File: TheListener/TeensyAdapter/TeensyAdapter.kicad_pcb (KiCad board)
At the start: 2 copper layers, 19 parts, among them J1 Conn_02x05_Odd_Even, J2 Conn_02x05_Odd_Even, U1 Teensy3.5

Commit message: updates
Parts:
- moved R16 6.00 mm to (159.0, 130.8), turned to 90 degrees
- moved R11 6.00 mm to (176.8, 140.2), turned to 270 degrees
- moved R4 6.00 mm to (153.9, 140.2), turned to 90 degrees
- moved R6 6.00 mm to (159.0, 140.2), turned to 90 degrees
- moved R8 6.00 mm to (164.1, 140.2), turned to 90 degrees
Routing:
- net R_8: track 0.00 -> 32.9 mm
- net T_6: track 22.0 -> 4.25 mm
- net R_4: track 10.0 -> 3.92 mm
- net T_7: track 14.2 -> 8.75 mm
- net T_3: track 11.1 -> 16.3 mm
- net T_1: track 5.73 -> 10.1 mm
- net R_7: track 10.2 -> 6.37 mm
- net R_1: track 0.00 -> 3.54 mm
- net R_2: track 17.9 -> 21.1 mm
- net T_4: track 12.9 -> 15.7 mm
- net R_6: track 32.4 -> 30.0 mm
- net Net-(R9-Pad1): track 2.34 -> 0.00 mm
- net Net-(R8-Pad1): track 2.34 -> 0.00 mm
- net Net-(R7-Pad1): track 2.34 -> 0.00 mm
- net Net-(R6-Pad1): track 2.34 -> 0.00 mm
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
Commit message: working
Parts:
- added J3: Conn_01x04_Male, Connector_PinHeader_2.54mm:PinHeader_1x04_P2.54mm_Vertical, F.Cu at (149.9, 139.7)
- added J4: Conn_01x04_Male, Connector_PinHeader_2.54mm:PinHeader_1x04_P2.54mm_Vertical, F.Cu at (175.3, 129.5)
- moved R16 7.09 mm to (157.5, 123.8), turned to 270 degrees
- moved R7 6.73 mm to (160.0, 139.7), turned to 90 degrees
- moved J1 6.13 mm to (154.9, 139.7)
- moved R11 5.27 mm to (175.3, 145.3), turned to 90 degrees
- moved R6 5.27 mm to (157.5, 145.3), turned to 270 degrees
- moved R4 5.27 mm to (152.4, 145.3), turned to 270 degrees
- moved R14 5.03 mm to (165.1, 129.5), turned to 270 degrees
- moved R5 1.83 mm to (154.9, 145.3)
- moved R1 1.82 mm to (144.8, 145.3)
- moved R2 1.82 mm to (147.3, 145.3)
- moved R9 1.82 mm to (165.1, 145.3)
- moved R10 1.82 mm to (170.2, 145.3)
- moved R3 1.82 mm to (149.9, 145.3)
- moved R13 1.81 mm to (167.6, 123.8)
- moved R15 1.81 mm to (154.9, 123.8)
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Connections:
- J1 pad 1: T_5 -> R_5
- J1 pad 2: R_5 -> T_6
- J1 pad 3: GND -> T_5
- J1 pad 4: T_6 -> R_6
- J1 pad 5: +5V -> (no net)
- J1 pad 6: R_6 -> (no net)
- J2 pad 1: T_1 -> R_1
- J2 pad 2: R_1 -> T_2
- J2 pad 3: GND -> T_1
- J2 pad 4: T_2 -> R_2
- J2 pad 5: +5V -> (no net)
- J2 pad 6: R_2 -> (no net)
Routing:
- net R_6: track 30.0 -> 1.82 mm
- net R_8: track 32.9 -> 17.4 mm
- net R_7: track 6.37 -> 17.4 mm
- net +5V: track 0.00 -> 9.72 mm
- net T_3: track 16.3 -> 6.99 mm
- net R_4: track 3.92 -> 10.3 mm
- net T_8: track 11.8 -> 6.07 mm
- net T_5: track 6.15 -> 10.5 mm
- net T_7: track 8.75 -> 12.8 mm
- net R_1: track 3.54 -> 6.86 mm
- net T_2: track 8.94 -> 6.28 mm
- net T_4: track 15.7 -> 13.1 mm
- net Net-(R3-Pad1): track 2.34 -> 0.00 mm
- net Net-(R2-Pad1): track 2.34 -> 0.00 mm
- net Net-(R14-Pad1): track 2.34 -> 0.00 mm
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
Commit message: working
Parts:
- moved R14 5.71 mm to (165.1, 123.8), turned to 90 degrees
- moved R7 5.59 mm to (160.0, 145.3), turned to 270 degrees
- moved R8 5.59 mm to (162.6, 145.3), turned to 270 degrees
- moved J2 5.08 mm to (165.1, 129.5)
- moved J3 5.08 mm to (144.8, 139.7)
- moved J1 5.08 mm to (149.9, 139.7)
- moved J4 5.08 mm to (170.2, 129.5)
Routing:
- net R_6: track 1.82 -> 16.9 mm
- net R_2: track 22.2 -> 10.2 mm
- net R_3: track 6.22 -> 18.1 mm
- net R_1: track 6.86 -> 18.3 mm
- net +5V: track 9.72 -> 0.00 mm
- net T_3: track 6.99 -> 16.1 mm
- net T_4: track 13.1 -> 6.07 mm
- net R_4: track 10.3 -> 17.2 mm
- net R_7: track 17.4 -> 10.5 mm
- net T_6: track 4.35 -> 9.68 mm
- net T_7: track 12.8 -> 8.00 mm
- net T_2: track 6.28 -> 10.4 mm
- net T_8: track 6.07 -> 9.97 mm
- net R_8: track 17.4 -> 15.2 mm
- net T_1: track 10.6 -> 8.83 mm
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
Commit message: updates
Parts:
- moved R3 6.86 mm to (149.9, 138.4), turned to 90 degrees
- moved R6 6.86 mm to (157.5, 138.4), turned to 90 degrees
- moved R7 6.86 mm to (160.0, 138.4), turned to 90 degrees
- moved R8 6.86 mm to (162.6, 138.4), turned to 90 degrees
- moved R16 4.45 mm to (157.5, 128.3), turned to 90 degrees
- moved J1 2.84 mm to (152.4, 138.4)
- moved J2 2.84 mm to (167.6, 128.3)
- moved J3 2.84 mm to (147.3, 138.4)
- moved J4 2.84 mm to (172.7, 128.3)
- moved R1 1.27 mm to (144.8, 144.0)
- moved R10 1.27 mm to (170.2, 144.0)
- moved R11 1.27 mm to (175.3, 144.0)
- moved R2 1.27 mm to (147.3, 144.0)
- moved R4 1.27 mm to (152.4, 144.0)
- moved R5 1.27 mm to (154.9, 144.0)
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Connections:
- U1 pad 1: (no net) -> GND
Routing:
- net GND: track 0.00 -> 11.4 mm
- net +5V: track 0.00 -> 10.4 mm
- net T_2: track 10.4 -> 1.56 mm
- net T_6: track 9.68 -> 1.92 mm
- net T_1: track 8.83 -> 2.58 mm
- net T_7: track 8.00 -> 2.17 mm
- net R_4: track 17.2 -> 11.6 mm
- net T_3: track 16.1 -> 10.5 mm
- net R_3: track 18.1 -> 13.2 mm
- net R_7: track 10.5 -> 15.1 mm
- net R_1: track 18.3 -> 22.4 mm
- net R_8: track 15.2 -> 11.1 mm
- net R_6: track 16.9 -> 13.9 mm
- net T_8: track 9.97 -> 7.66 mm
- net R_2: track 10.2 -> 12.2 mm
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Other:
- board outline added: 67.3 x 30 mm

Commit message: wip
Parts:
- removed J3, J4: Conn_01x04_Male, Connector_PinHeader_2.54mm:PinHeader_1x04_P2.54mm_Vertical
- moved R1 6.10 mm to (144.8, 137.9), turned to 90 degrees
- moved R3 0.51 mm to (149.9, 137.9)
- moved R6 0.51 mm to (157.5, 137.9)
- moved R7 0.51 mm to (160.0, 137.9)
- moved R8 0.51 mm to (162.6, 137.9)
- moved R16 0.51 mm to (157.5, 128.8)
- moved R12 0.13 mm to (172.7, 122.7)
- moved R13 0.13 mm to (167.6, 122.7)
- moved R14 0.13 mm to (165.1, 122.7)
- moved R15 0.13 mm to (154.9, 122.7)
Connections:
- J1 pad 5: (no net) -> +5V
- J1 pad 6: (no net) -> GND
- J2 pad 5: (no net) -> +5V
- J2 pad 6: (no net) -> GND
- R1 pad 2: R_8 -> R_4
- R10 pad 2: R_3 -> R_7
- R11 pad 1: R_4 -> R_8
- R12 pad 2: T_5 -> T_1
- R13 pad 2: R_5 -> R_1
- R14 pad 2: R_6 -> R_3
- R15 pad 1: T_8 -> T_4
- R16 pad 1: T_7 -> T_3
- R2 pad 2: R_7 -> R_5
- R3 pad 2: T_1 -> T_5
- R4 pad 2: R_1 -> R_2
- R5 pad 2: R_2 -> R_6
- R6 pad 2: T_2 -> T_6
- R7 pad 2: T_3 -> T_2
- R8 pad 2: T_6 -> T_7
- R9 pad 2: T_4 -> T_8
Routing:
- net +5V: track 10.4 -> 110.0 mm
- net R_1: track 22.4 -> 6.63 mm
- net R_2: track 12.2 -> 23.8 mm
- net GND: track 11.4 -> 0.00 mm
- net T_2: track 1.56 -> 11.0 mm
- net T_1: track 2.58 -> 11.0 mm
- net T_5: track 10.9 -> 3.31 mm
- net T_3: track 10.5 -> 3.31 mm
- net Net-(R9-Pad1): track 0.00 -> 2.29 mm
- net Net-(R8-Pad1): track 0.00 -> 2.29 mm
- net Net-(R7-Pad1): track 0.00 -> 2.29 mm
- net Net-(R6-Pad1): track 0.00 -> 2.29 mm
- net Net-(R5-Pad1): track 0.00 -> 2.29 mm
- net Net-(R4-Pad1): track 0.00 -> 2.29 mm
- net Net-(R3-Pad1): track 0.00 -> 2.29 mm
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- added copper zone on B.Cu, net GND
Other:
- board size 67.3 x 30 mm -> 63.5 x 28.3 mm

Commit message: wip
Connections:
- J1 pad 5: +5V -> GND
- J2 pad 5: +5V -> GND
- U1 pad 53: +5V -> (no net)
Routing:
- net +5V: track 110.0 -> 0.00 mm
- net R_4: track 12.4 -> 10.2 mm, vias 2 -> 0
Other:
- board size 63.5 x 28.3 mm -> 63.5 x 36.8 mm

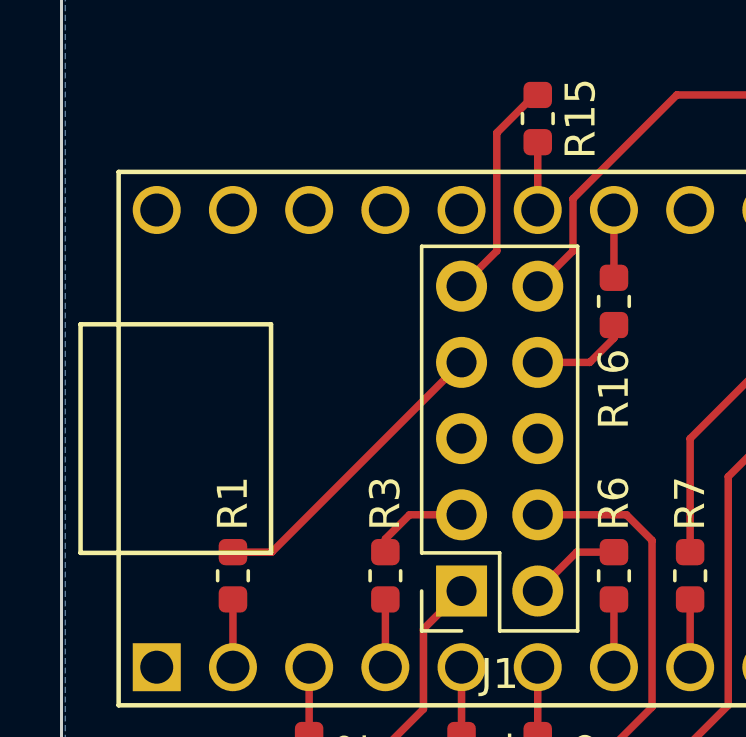
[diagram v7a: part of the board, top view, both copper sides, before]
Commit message: updates to add power correctly
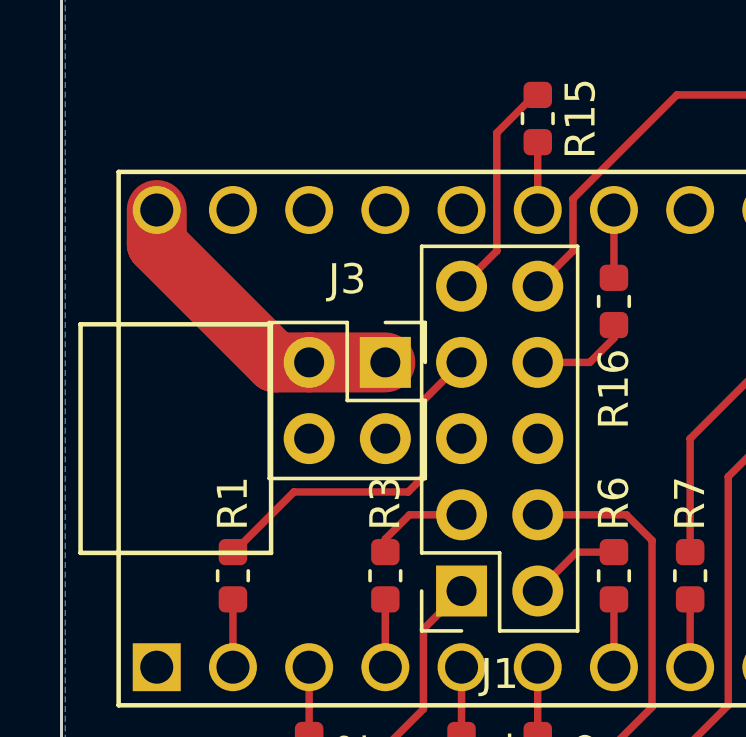
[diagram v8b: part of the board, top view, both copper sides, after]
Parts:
- added J3: Conn_02x02_Odd_Even, TheListener:PinSocket_2x02_P2.54mm_Vertical_MinCrtYd, F.Cu at (149.9, 130.8)
- J1, J2: footprint Connector_PinSocket_2.54mm:PinSocket_2x05_P2.54mm_Vertical -> TheListener:PinSocket_2x05_P2.54mm_Vertical_MinCrtYd
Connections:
- U1 pad 53: (no net) -> +5V
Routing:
- net +5V: track 0.00 -> 10.4 mm
- net R_4: track 10.2 -> 11.7 mm
